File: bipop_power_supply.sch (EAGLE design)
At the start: 27 parts, among them IC1 LM1117MP-3.3, IC2 LM1117MP-5.0, X2 MSTBA6

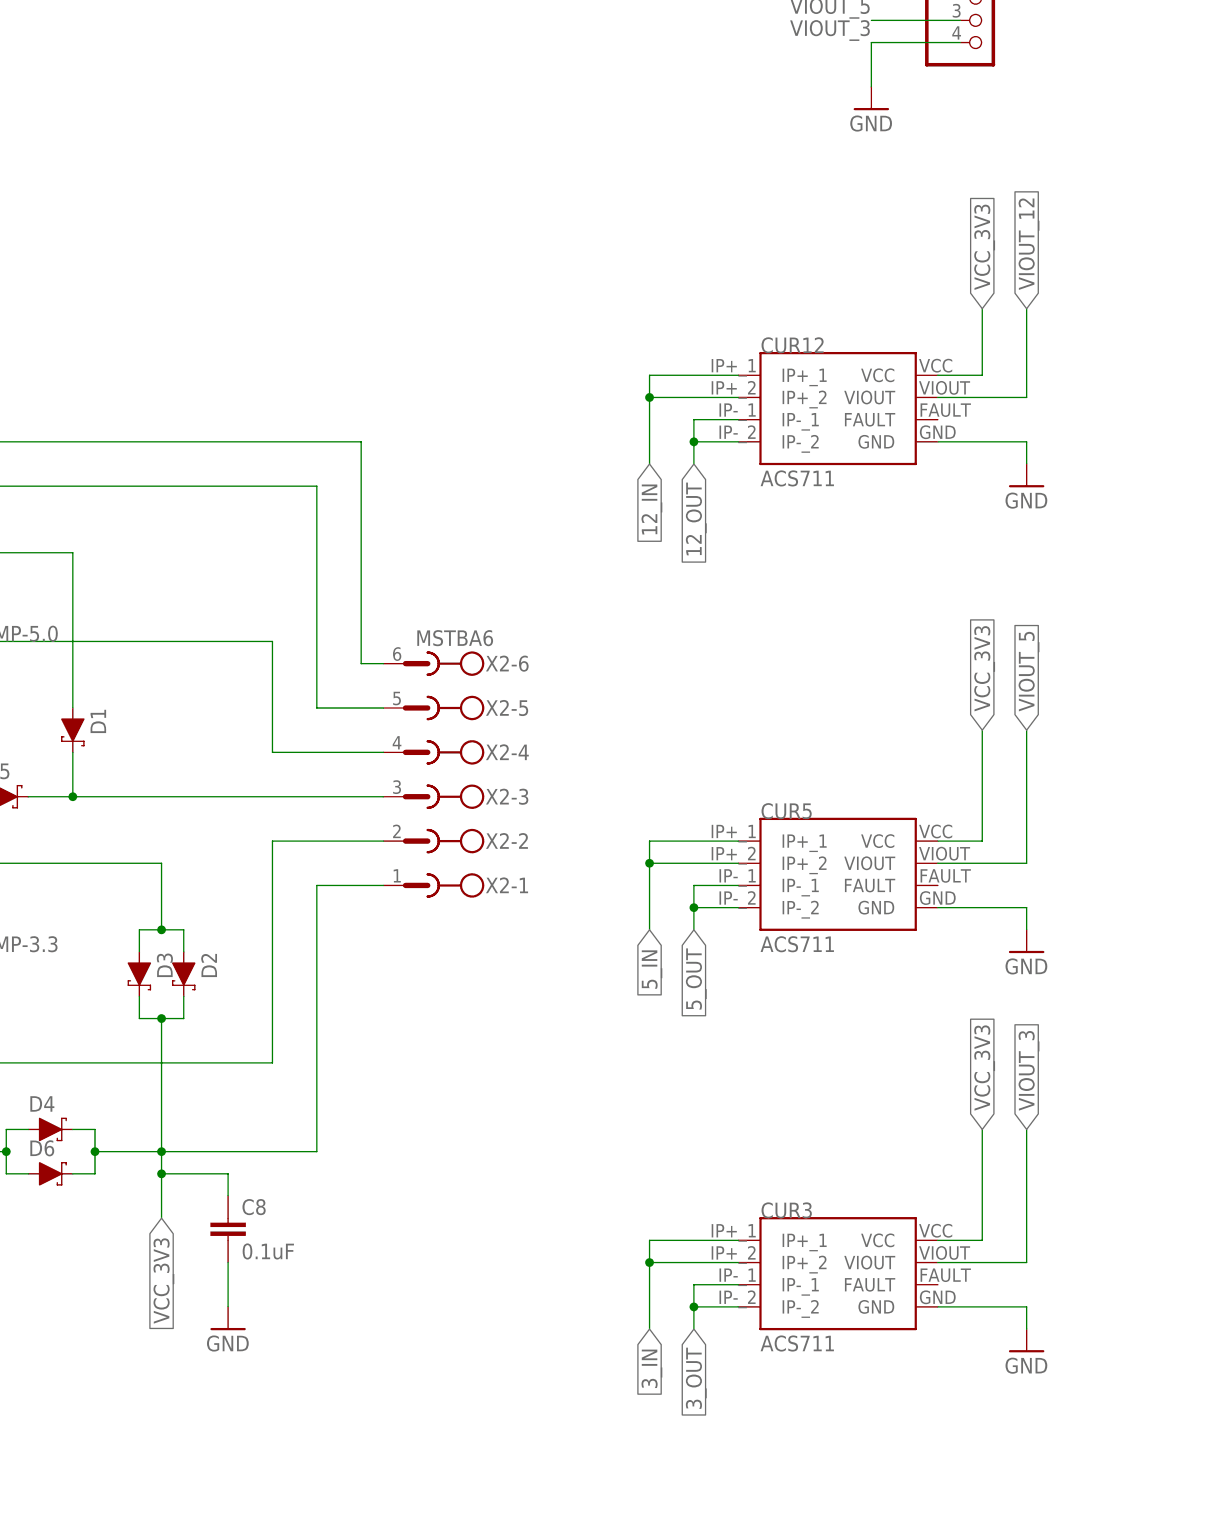
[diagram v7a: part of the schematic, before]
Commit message: poprawione, dodane pullupy do czujnikow pradu
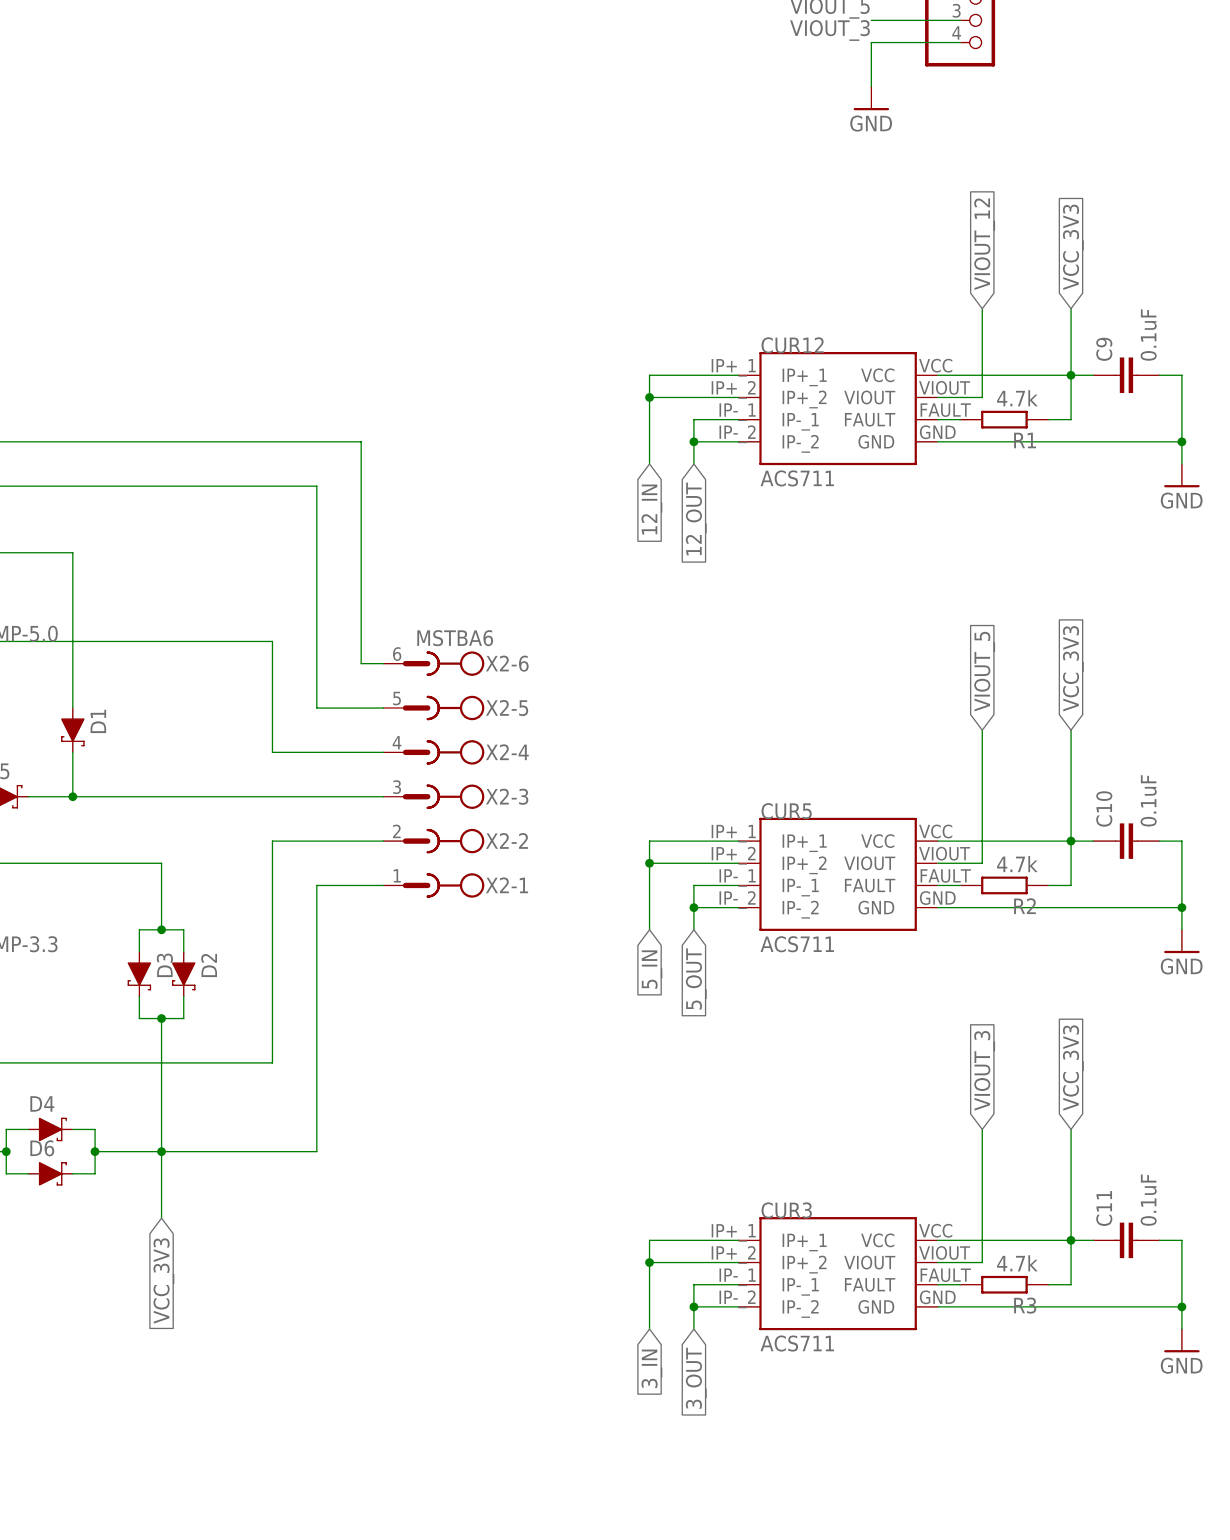
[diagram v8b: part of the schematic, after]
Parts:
- removed C8: 0.1uF, rcl:C-EUC0805
- added C10, C11, C9: 0.1uF, rcl:C-EUC0805
- added R1, R2, R3: 4.7k, resistor:R-EU_R0805
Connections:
- new net N$1: CUR12.FAULT, R1.2
- new net N$4: CUR5.FAULT, R2.2
- new net N$7: CUR3.FAULT, R3.2
- net GND: now also C10.2, C11.2, C9.2; no longer C8.2
- net VCC_3V3: now also C10.1, C11.1, C9.1, R1.1, R2.1, R3.1; no longer C8.1
